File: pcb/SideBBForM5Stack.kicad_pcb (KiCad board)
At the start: 2 copper layers, 100 x 50 mm, 15 parts, among them J1 Conn_01x15, J2 Conn_01x15, J3 Conn_02x15_Odd_Even, J4 Conn_02x15_Odd_Even

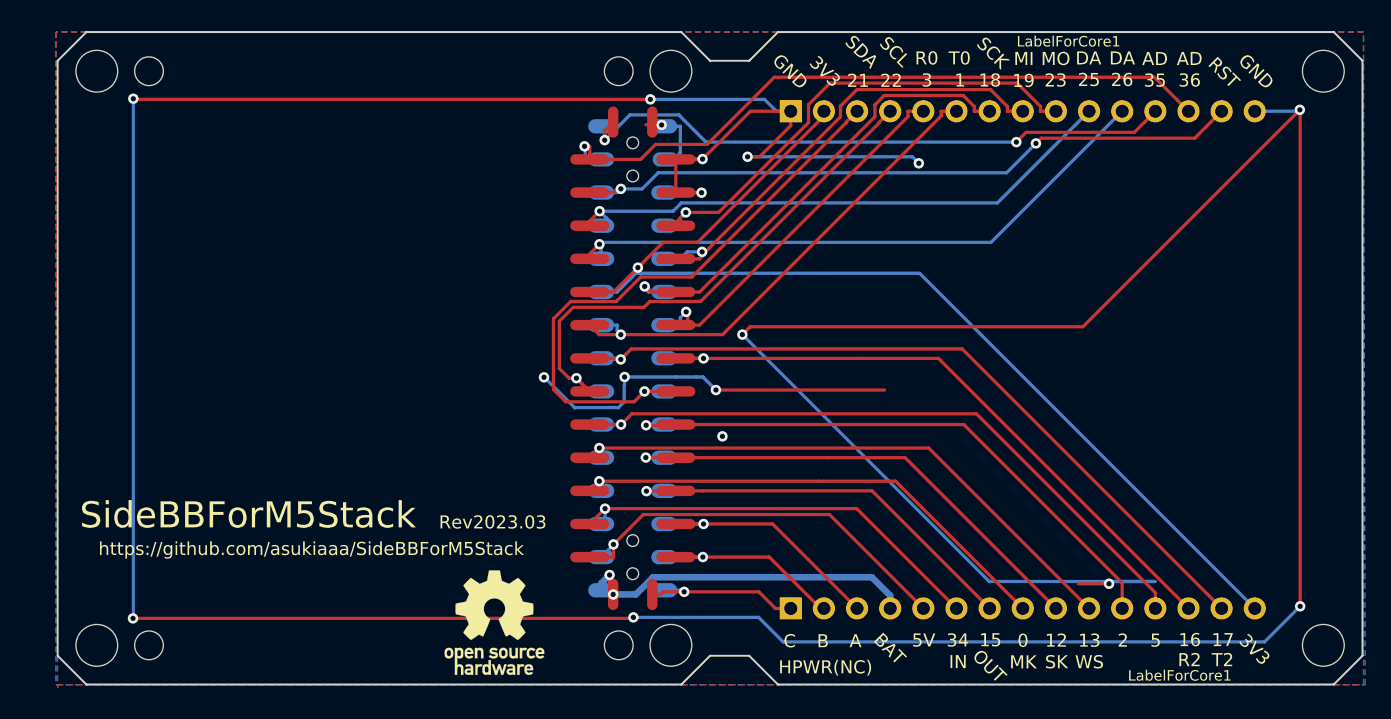
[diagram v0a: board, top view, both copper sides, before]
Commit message: Move header and socket position 0.03mm inside as rev2024.01
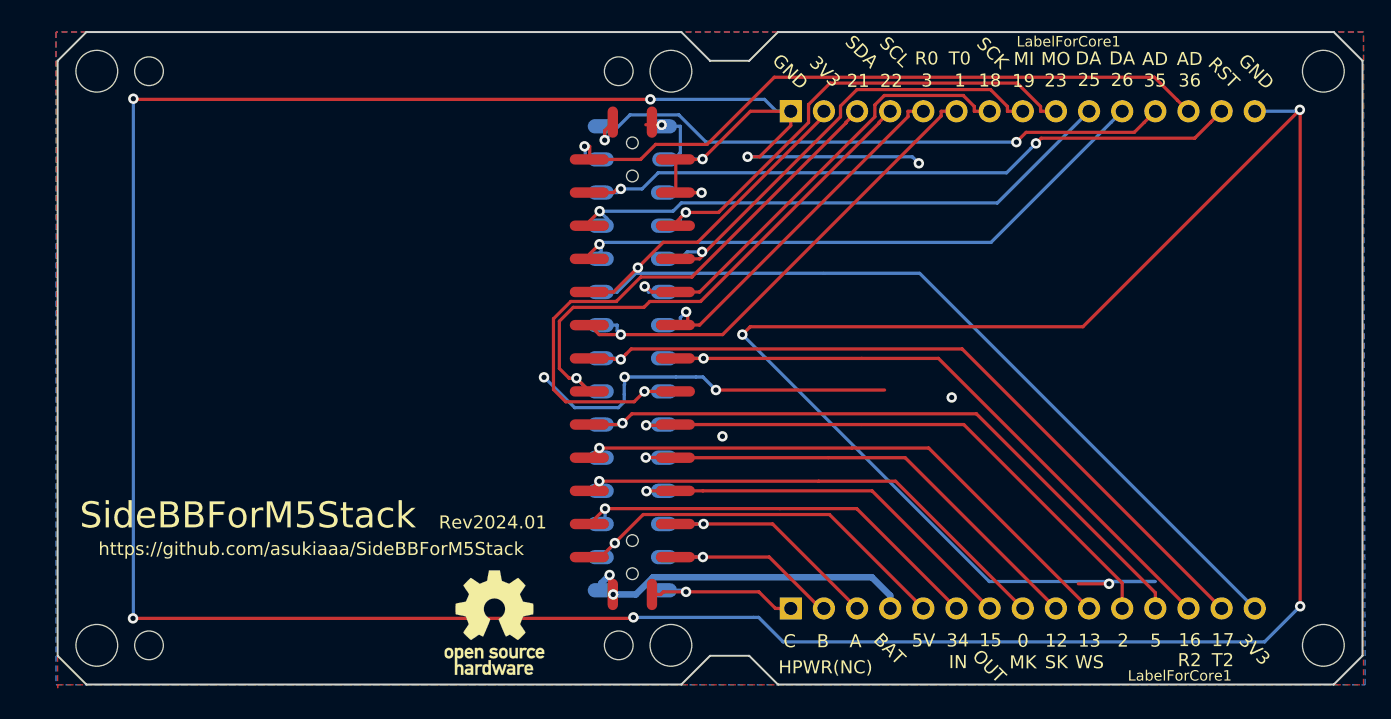
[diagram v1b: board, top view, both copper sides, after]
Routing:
- net GND: vias 17 -> 18
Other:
- board text added: "Rev2024.01"
- board text removed: "Rev2023.03"
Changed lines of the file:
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@@
   )
   (footprint "footprints:PinHeader_2x15_P2.54mm_M5Stack_SpacerPCB_pads" (layer "F.Cu")
-    (at 144.074 75)
+    (at 144.044 75)
     (descr "surface-mounted straight pin header, 2x15, 2.54mm pitch, double rows")
     (tags "Surface mounted pin header SMD 2x15 2.54mm double row")
@@
   )
   (footprint "footprints:PinSocket_2x15_P2.54mm_Vertical_SMD_just_for_M5Stack_bottom" (layer "B.Cu")
-    (at 144.074 75 180)
+    (at 144.044 75 180)
     (descr "surface-mounted straight socket strip, 2x15, 2.54mm pitch, double cols (from Kicad 4.0.7), script generated")
     (tags "Surface mounted socket strip SMD 2x15 2.54mm double row")
@@
     (effects (font (size 2.5 2.5) (thickness 0.625)) (justify mirror))
   )
-  (gr_text "Rev2023.03" (at 158.1988 87.8832) (layer "B.SilkS")
+  (gr_text "Rev2024.01" (at 158.1988 87.8832) (layer "B.SilkS")
     (effects (font (size 1.2 1.2) (thickness 0.3)) (justify mirror))
   )
@@
     (effects (font (size 1 1) (thickness 0.25)))
   )
-  (gr_text "Rev2023.03" (at 133.3488 87.5792) (layer "F.SilkS")
+  (gr_text "Rev2024.01" (at 133.3488 87.5792) (layer "F.SilkS")
     (effects (font (size 1 1) (thickness 0.25)))
   )
@@
   (via (at 150.9488 80.9832) (size 0.8) (drill 0.4) (layers "F.Cu" "B.Cu") (net 1))
   (via (at 143.4488 76.4332) (size 0.8) (drill 0.4) (layers "F.Cu" "B.Cu") (net 1))
+  (via (at 168.5188 78.0032) (size 0.8) (drill 0.4) (layers "F.Cu" "B.Cu") (free) (net 1))
   (via (at 137.27398 76.4582) (size 0.8) (drill 0.4) (layers "F.Cu" "B.Cu") (net 1))
   (via (at 150.4488 77.4332) (size 0.8) (drill 0.4) (layers "F.Cu" "B.Cu") (net 1))
@@
   (segment (start 163.805 93.1894) (end 163.805 94.17) (width 0.5) (layer "B.Cu") (net 11))
   (segment (start 142.254 92.78) (end 142.574 93.1) (width 0.25) (layer "B.Cu") (net 11))
-  (segment (start 159.1484 86.9734) (end 144.89 86.9734) (width 0.25) (layer "F.Cu") (net 12))
-  (segment (start 140.774 90.24) (end 142.5993 90.24) (width 0.25) (layer "F.Cu") (net 12))
-  (segment (start 142.5993 89.2641) (end 142.5993 90.24) (width 0.25) (layer "F.Cu") (net 12))
-  (segment (start 144.89 86.9734) (end 142.5993 89.2641) (width 0.25) (layer "F.Cu") (net 12))
-  (segment (start 166.345 94.17) (end 159.1484 86.9734) (width 0.25) (layer "F.Cu") (net 12))
-  (via (at 142.5993 89.2641) (size 0.8) (drill 0.4) (layers "F.Cu" "B.Cu") (net 12))
-  (segment (start 142.5993 89.2641) (end 142.5993 89.2947) (width 0.25) (layer "B.Cu") (net 12))
-  (segment (start 142.5993 89.2947) (end 141.654 90.24) (width 0.25) (layer "B.Cu") (net 12))
+  (segment (start 142.6995 89.147774) (end 144.873874 86.9734) (width 0.25) (layer "F.Cu") (net 12))
+  (segment (start 142.6995 89.1639) (end 141.6234 90.24) (width 0.25) (layer "F.Cu") (net 12))
+  (segment (start 159.1484 86.9734) (end 166.345 94.17) (width 0.25) (layer "F.Cu") (net 12))
+  (segment (start 144.873874 86.9734) (end 159.1484 86.9734) (width 0.25) (layer "F.Cu") (net 12))
+  (segment (start 141.6234 90.24) (end 140.774 90.24) (width 0.25) (layer "F.Cu") (net 12))
+  (segment (start 142.6995 89.1639) (end 142.6995 89.147774) (width 0.25) (layer "F.Cu") (net 12))
+  (via (at 142.6995 89.1639) (size 0.8) (drill 0.4) (layers "F.Cu" "B.Cu") (net 12))
+  (segment (start 142.6995 89.1639) (end 142.6995 89.1945) (width 0.25) (layer "B.Cu") (net 12))
+  (segment (start 142.6995 89.1945) (end 141.654 90.24) (width 0.25) (layer "B.Cu") (net 12))
   (segment (start 141.9509 86.5231) (end 140.774 87.7) (width 0.25) (layer "F.Cu") (net 13))
   (segment (start 155.3501 86.5231) (end 141.9509 86.5231) (width 0.25) (layer "F.Cu") (net 13))
@@
   (segment (start 141.5133 82.4793) (end 141.654 82.62) (width 0.25) (layer "B.Cu") (net 15))
   (segment (start 141.5133 81.8807) (end 141.5133 82.4793) (width 0.25) (layer "B.Cu") (net 15))
-  (segment (start 184.125 92.967919) (end 170.411781 79.2547) (width 0.25) (layer "F.Cu") (net 16))
-  (segment (start 184.125 94.17) (end 184.125 92.967919) (width 0.25) (layer "F.Cu") (net 16))
-  (segment (start 170.411781 79.2547) (end 144.0047 79.2547) (width 0.25) (layer "F.Cu") (net 16))
-  (segment (start 140.774 80.08) (end 142.5993 80.08) (width 0.25) (layer "F.Cu") (net 16))
-  (segment (start 144.0047 79.2547) (end 143.1794 80.08) (width 0.25) (layer "F.Cu") (net 16))
-  (segment (start 142.5993 80.08) (end 143.1794 80.08) (width 0.25) (layer "F.Cu") (net 16))
-  (via (at 143.1794 80.08) (size 0.8) (drill 0.4) (layers "F.Cu" "B.Cu") (net 16))
-  (segment (start 142.8793 80.08) (end 143.1794 80.08) (width 0.25) (layer "B.Cu") (net 16))
-  (segment (start 141.654 80.08) (end 142.8793 80.08) (width 0.25) (layer "B.Cu") (net 16))
+  (segment (start 184.125 92.967919) (end 184.125 94.17) (width 0.25) (layer "F.Cu") (net 16))
+  (segment (start 143.2875 79.9719) (end 143.1794 80.08) (width 0.25) (layer "F.Cu") (net 16))
+  (segment (start 143.2875 79.9719) (end 144.0047 79.2547) (width 0.25) (layer "F.Cu") (net 16))
+  (segment (start 143.1794 80.08) (end 140.774 80.08) (width 0.25) (layer "F.Cu") (net 16))
+  (segment (start 170.411781 79.2547) (end 184.125 92.967919) (width 0.25) (layer "F.Cu") (net 16))
+  (segment (start 144.0047 79.2547) (end 170.411781 79.2547) (width 0.25) (layer "F.Cu") (net 16))
+  (via (at 143.2875 79.9719) (size 0.8) (drill 0.4) (layers "F.Cu" "B.Cu") (net 16))
+  (segment (start 143.2875 79.9719) (end 143.1794 80.08) (width 0.25) (layer "B.Cu") (net 16))
+  (segment (start 143.1794 80.08) (end 141.654 80.08) (width 0.25) (layer "B.Cu") (net 16))
   (segment (start 140.7734 77.54) (end 140.774 77.54) (width 0.25) (layer "F.Cu") (net 17))
   (segment (start 145.3847 70.6453) (end 149.274018 70.6453) (width 0.25) (layer "F.Cu") (net 17))
@@
   (segment (start 144.3111 68.4882) (end 142.8793 69.92) (width 0.25) (layer "B.Cu") (net 25))
   (segment (start 166.0632 68.4882) (end 158.725 68.4882) (width 0.25) (layer "B.Cu") (net 25))
-  (segment (start 155.0097 94.17) (end 153.7397 92.9) (width 0.25) (layer "F.Cu") (net 26))
-  (segment (start 146.424 92.9) (end 147.374 92.9) (width 0.25) (layer "F.Cu") (net 26))
-  (segment (start 146.224 93.1) (end 146.424 92.9) (width 0.25) (layer "F.Cu") (net 26))
-  (segment (start 145.574 93.1) (end 146.224 93.1) (width 0.25) (layer "F.Cu") (net 26))
-  (segment (start 153.7397 92.9) (end 148.0156 92.9) (width 0.25) (layer "F.Cu") (net 26))
-  (segment (start 148.0156 92.9) (end 147.374 92.9) (width 0.25) (layer "F.Cu") (net 26))
-  (segment (start 156.185 94.17) (end 155.0097 94.17) (width 0.25) (layer "F.Cu") (net 26))
-  (via (at 148.0156 92.9) (size 0.8) (drill 0.4) (layers "F.Cu" "B.Cu") (net 26))
-  (segment (start 147.8956 92.78) (end 148.0156 92.9) (width 0.25) (layer "B.Cu") (net 26))
-  (segment (start 146.494 92.78) (end 147.8956 92.78) (width 0.25) (layer "B.Cu") (net 26))
-  (segment (start 147.3808 90.2332) (end 147.374 90.24) (width 0.25) (layer "F.Cu") (net 27))
+  (segment (start 148.1588 92.9) (end 153.7397 92.9) (width 0.25) (layer "F.Cu") (net 26))
+  (segment (start 146.424 92.9) (end 146.224 93.1) (width 0.25) (layer "F.Cu") (net 26))
+  (segment (start 148.1588 92.9) (end 146.424 92.9) (width 0.25) (layer "F.Cu") (net 26))
+  (segment (start 153.7397 92.9) (end 155.0097 94.17) (width 0.25) (layer "F.Cu") (net 26))
+  (segment (start 155.0097 94.17) (end 156.185 94.17) (width 0.25) (layer "F.Cu") (net 26))
+  (segment (start 146.224 93.1) (end 145.574 93.1) (width 0.25) (layer "F.Cu") (net 26))
+  (via (at 148.1588 92.9) (size 0.8) (drill 0.4) (layers "F.Cu" "B.Cu") (net 26))
+  (segment (start 148.0388 92.78) (end 146.494 92.78) (width 0.25) (layer "B.Cu") (net 26))
+  (segment (start 148.1588 92.9) (end 148.0388 92.78) (width 0.25) (layer "B.Cu") (net 26))
+  (segment (start 149.4488 90.2332) (end 154.533202 90.2332) (width 0.25) (layer "F.Cu") (net 27))
   (segment (start 149.4488 90.2332) (end 147.3808 90.2332) (width 0.25) (layer "F.Cu") (net 27))
   (segment (start 158.470002 94.17) (end 158.725 94.17) (width 0.25) (layer "F.Cu") (net 27))
   (segment (start 154.533202 90.2332) (end 158.470002 94.17) (width 0.25) (layer "F.Cu") (net 27))
-  (segment (start 149.4488 90.2332) (end 154.533202 90.2332) (width 0.25) (layer "F.Cu") (net 27))
+  (segment (start 147.3808 90.2332) (end 147.374 90.24) (width 0.25) (layer "F.Cu") (net 27))
   (via (at 149.4488 90.2332) (size 0.8) (drill 0.4) (layers "F.Cu" "B.Cu") (net 27))
-  (segment (start 146.494 90.24) (end 149.442 90.24) (width 0.25) (layer "B.Cu") (net 27))
-  (segment (start 149.442 90.24) (end 149.4488 90.2332) (width 0.25) (layer "B.Cu") (net 27))
+  (segment (start 149.4488 90.2332) (end 149.442 90.24) (width 0.25) (layer "B.Cu") (net 27))
+  (segment (start 149.442 90.24) (end 146.494 90.24) (width 0.25) (layer "B.Cu") (net 27))
   (segment (start 149.4972 87.7) (end 149.4988 87.6984) (width 0.25) (layer "F.Cu") (net 28))
   (segment (start 149.4988 87.6984) (end 154.7934 87.6984) (width 0.25) (layer "F.Cu") (net 28))

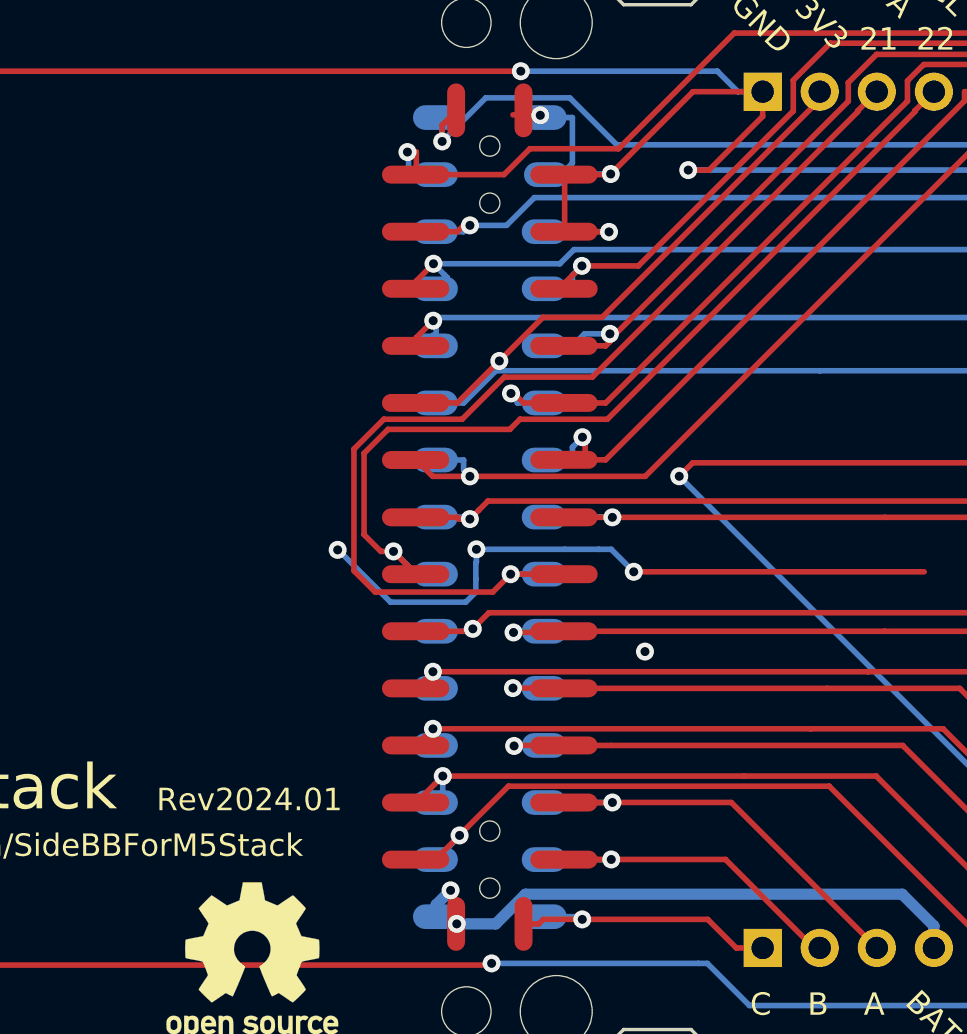
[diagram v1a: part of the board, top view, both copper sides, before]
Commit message: Expand hole size to 1.0 from 0.9mm
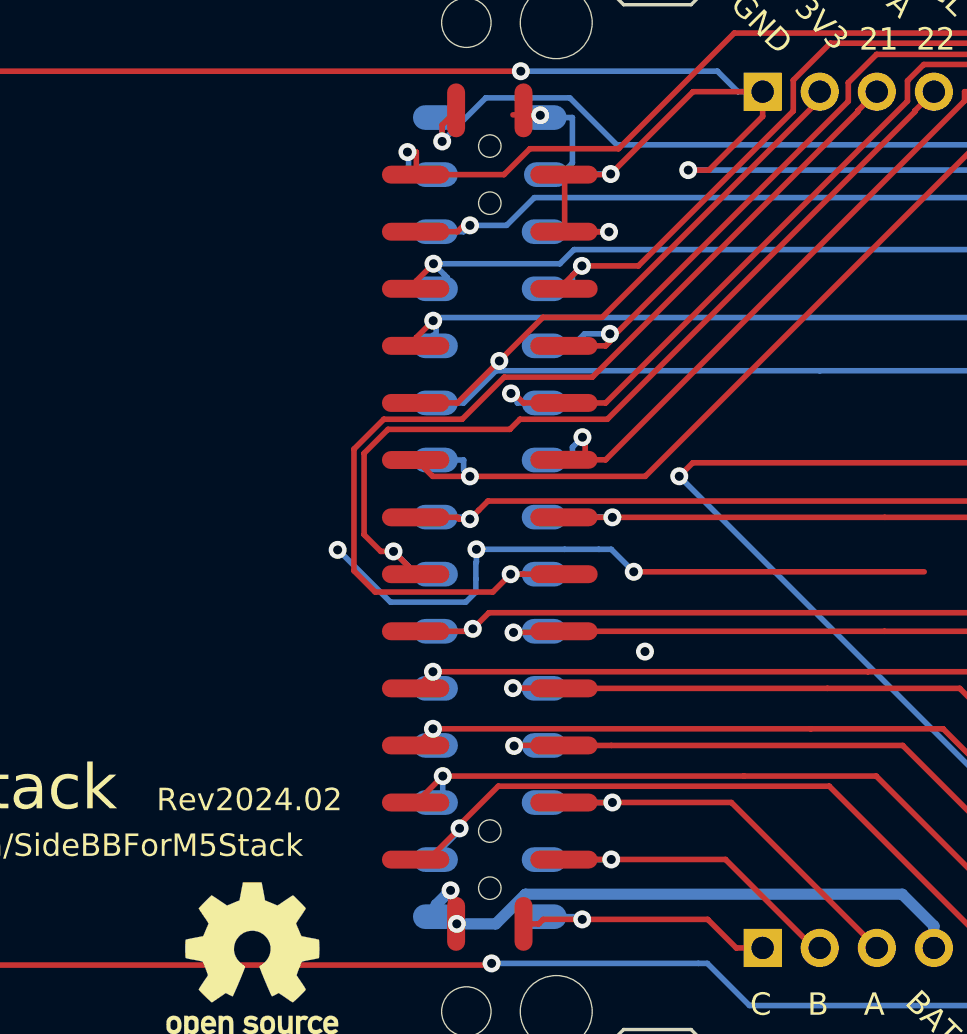
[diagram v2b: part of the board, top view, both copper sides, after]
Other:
- board text added: "Rev2024.02"
- board text removed: "Rev2024.01"
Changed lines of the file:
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@@
     (fp_line (start 3.6 18.1) (end 2.54 18.1)
       (stroke (width 0.1) (type solid)) (layer "F.Fab"))
-    (pad "" np_thru_hole oval (at 0 -13.97) (size 0.9 0.9) (drill 0.9) (layers "*.Cu" "*.Mask"))
-    (pad "" np_thru_hole oval (at 0 13.97) (size 0.9 0.9) (drill 0.9) (layers "*.Cu" "*.Mask"))
+    (pad "" np_thru_hole oval (at 0 -13.97) (size 0.9 0.9) (drill 1) (layers "F&B.Cu" "*.Mask"))
+    (pad "" np_thru_hole oval (at 0 13.97) (size 0.9 0.9) (drill 1) (layers "F&B.Cu" "*.Mask"))
     (pad "1" smd oval (at -1.5 -18.1 90) (size 2.4 0.8) (layers "F.Cu" "F.Paste" "F.Mask")
       (net 24 "G35"))
@@
     (fp_line (start 3.92 18.1) (end 3.92 17.46)
       (stroke (width 0.1) (type solid)) (layer "B.Fab"))
-    (pad "" np_thru_hole circle (at 0 -16.51 180) (size 0.9 0.9) (drill 0.9) (layers "*.Cu" "*.Mask"))
-    (pad "" np_thru_hole circle (at 0 16.51 180) (size 0.9 0.9) (drill 0.9) (layers "*.Cu" "*.Mask"))
+    (pad "" np_thru_hole circle (at 0 -16.51 180) (size 0.9 0.9) (drill 1) (layers "F&B.Cu" "*.Mask"))
+    (pad "" np_thru_hole circle (at 0 16.51 180) (size 0.9 0.9) (drill 1) (layers "F&B.Cu" "*.Mask"))
     (pad "1" smd oval (at 2.42 17.78 180) (size 2 1.1) (layers "B.Cu" "B.Paste" "B.Mask")
       (net 24 "G35"))
@@
     (effects (font (size 2.5 2.5) (thickness 0.625)) (justify mirror))
   )
-  (gr_text "Rev2024.01" (at 158.1988 87.8832) (layer "B.SilkS")
+  (gr_text "Rev2024.02" (at 158.1988 87.8832) (layer "B.SilkS")
     (effects (font (size 1.2 1.2) (thickness 0.3)) (justify mirror))
   )
@@
     (effects (font (size 1 1) (thickness 0.25)))
   )
-  (gr_text "Rev2024.01" (at 133.3488 87.5792) (layer "F.SilkS")
+  (gr_text "Rev2024.02" (at 133.3488 87.5792) (layer "F.SilkS")
     (effects (font (size 1 1) (thickness 0.25)))
   )
@@
   (segment (start 163.805 93.1894) (end 163.805 94.17) (width 0.5) (layer "B.Cu") (net 11))
   (segment (start 142.254 92.78) (end 142.574 93.1) (width 0.25) (layer "B.Cu") (net 11))
-  (segment (start 142.6995 89.147774) (end 144.873874 86.9734) (width 0.25) (layer "F.Cu") (net 12))
-  (segment (start 142.6995 89.1639) (end 141.6234 90.24) (width 0.25) (layer "F.Cu") (net 12))
+  (segment (start 141.3087 90.24) (end 140.774 90.24) (width 0.25) (layer "F.Cu") (net 12))
+  (segment (start 142.6995 88.8492) (end 141.3087 90.24) (width 0.25) (layer "F.Cu") (net 12))
   (segment (start 159.1484 86.9734) (end 166.345 94.17) (width 0.25) (layer "F.Cu") (net 12))
-  (segment (start 144.873874 86.9734) (end 159.1484 86.9734) (width 0.25) (layer "F.Cu") (net 12))
-  (segment (start 141.6234 90.24) (end 140.774 90.24) (width 0.25) (layer "F.Cu") (net 12))
-  (segment (start 142.6995 89.1639) (end 142.6995 89.147774) (width 0.25) (layer "F.Cu") (net 12))
-  (via (at 142.6995 89.1639) (size 0.8) (drill 0.4) (layers "F.Cu" "B.Cu") (net 12))
-  (segment (start 142.6995 89.1639) (end 142.6995 89.1945) (width 0.25) (layer "B.Cu") (net 12))
-  (segment (start 142.6995 89.1945) (end 141.654 90.24) (width 0.25) (layer "B.Cu") (net 12))
+  (segment (start 142.6995 88.6945) (end 144.4206 86.9734) (width 0.25) (layer "F.Cu") (net 12))
+  (segment (start 144.4206 86.9734) (end 159.1484 86.9734) (width 0.25) (layer "F.Cu") (net 12))
+  (segment (start 142.6995 88.8492) (end 142.6995 88.6945) (width 0.25) (layer "F.Cu") (net 12))
+  (via (at 142.6995 88.8492) (size 0.8) (drill 0.4) (layers "F.Cu" "B.Cu") (net 12))
+  (segment (start 142.6995 88.9485) (end 141.654 89.994) (width 0.25) (layer "B.Cu") (net 12))
+  (segment (start 141.654 89.994) (end 141.654 90.24) (width 0.25) (layer "B.Cu") (net 12))
+  (segment (start 142.6995 88.8492) (end 142.6995 88.9485) (width 0.25) (layer "B.Cu") (net 12))
   (segment (start 141.9509 86.5231) (end 140.774 87.7) (width 0.25) (layer "F.Cu") (net 13))
   (segment (start 155.3501 86.5231) (end 141.9509 86.5231) (width 0.25) (layer "F.Cu") (net 13))
